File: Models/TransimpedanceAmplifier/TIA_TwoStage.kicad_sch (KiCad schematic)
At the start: 4 parts

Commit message: Save progress
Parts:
- added C_feedback: 80-220 fF, symbol Device:C
- R_feedback: renamed from R2; value 300M, 5% -> 330M, 5%; Purchase Link https://www.digikey.com/en/products/detail/vishay-dale/CRCW0603300MJPEAHR/5072019 -> https://www.digikey.com/en/products/detail/vishay-dale/CRCW0805330MJPEAHR/5074908
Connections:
- net at R_feedback.1: now also C_feedback.1
- net at R_feedback.2: now also C_feedback.2
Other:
- note added: "Noninverting Gain Stage Phase Shift: 0° Gain: 16.0 (-10 V < output < 10 V) 2.0 (outside ±10 V range)"
- moved on the sheet: RV1, RV2, RV3, R_feedback
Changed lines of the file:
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@@
 	(generator_version "9.0")
 	(paper "A4")
+	(text "Noninverting Gain Stage\n\nPhase Shift: 0°\n\nGain:\n16.0 (-10 V < output < 10 V)\n2.0 (outside ±10 V range)"
+		(exclude_from_sim no)
+		(at 152.908 67.818 0)
+		(effects
+			(font
+				(size 1.27 1.27)
+			)
+			(justify left)
+		)
+	)
+	(wire
+		(pts
+			(xy 77.47 53.34) (xy 73.66 53.34)
+		)
+		(stroke
+			(width 0)
+			(type default)
+		)
+	)
+	(wire
+		(pts
+			(xy 73.66 53.34) (xy 73.66 38.1)
+		)
+		(stroke
+			(width 0)
+			(type default)
+		)
+	)
+	(wire
+		(pts
+			(xy 73.66 38.1) (xy 77.47 38.1)
+		)
+		(stroke
+			(width 0)
+			(type default)
+		)
+	)
+	(wire
+		(pts
+			(xy 85.09 53.34) (xy 88.9 53.34)
+		)
+		(stroke
+			(width 0)
+			(type default)
+		)
+	)
+	(wire
+		(pts
+			(xy 85.09 38.1) (xy 88.9 38.1)
+		)
+		(stroke
+			(width 0)
+			(type default)
+		)
+	)
+	(wire
+		(pts
+			(xy 88.9 38.1) (xy 88.9 53.34)
+		)
+		(stroke
+			(width 0)
+			(type default)
+		)
+	)
+	(symbol
+		(lib_id "Device:C")
+		(at 81.28 38.1 90)
+		(unit 1)
+		(exclude_from_sim no)
+		(in_bom yes)
+		(on_board no)
+		(dnp no)
+		(fields_autoplaced yes)
+		(property "Reference" "C_feedback"
+			(at 81.28 30.48 90)
+			(effects
+				(font
+					(size 1.27 1.27)
+				)
+			)
+		)
+		(property "Value" "80-220 fF"
+			(at 81.28 33.02 90)
+			(effects
+				(font
+					(size 1.27 1.27)
+				)
+			)
+		)
+		(property "Footprint" ""
+			(at 85.09 37.1348 0)
+			(effects
+				(font
+					(size 1.27 1.27)
+				)
+				(hide yes)
+			)
+		)
+		(property "Datasheet" "~"
+			(at 81.28 38.1 0)
+			(effects
+				(font
+					(size 1.27 1.27)
+				)
+				(hide yes)
+			)
+		)
+		(property "Description" "Unpolarized capacitor"
+			(at 81.28 38.1 0)
+			(effects
+				(font
+					(size 1.27 1.27)
+				)
+				(hide yes)
+			)
+		)
+		(property "Purchase Link" ""
+			(at 81.28 38.1 0)
+			(effects
+				(font
+					(size 1.27 1.27)
+				)
+				(hide yes)
+			)
+		)
+		(pin "2"
+		)
+		(pin "1"
+		)
+		(instances
+			(project ""
+				(path "/ec9f2ae3-e40d-40eb-9760-2b611ee8efd1/226b3d0c-9e45-4bcf-9bef-58938aee743e"
+					(reference "C_feedback")
+					(unit 1)
+				)
+			)
+		)
+	)
 	(symbol
 		(lib_id "Device:R_US")
-		(at 91.44 53.34 0)
+		(at 81.28 53.34 90)
 		(unit 1)
 		(exclude_from_sim no)
@@
 		(dnp no)
 		(fields_autoplaced yes)
-		(property "Reference" "R2"
-			(at 93.98 52.0699 0)
-			(effects
-				(font
-					(size 1.27 1.27)
-				)
-				(justify left)
-			)
-		)
-		(property "Value" "300M, 5%"
-			(at 93.98 54.6099 0)
-			(effects
-				(font
-					(size 1.27 1.27)
-				)
-				(justify left)
+		(property "Reference" "R_feedback"
+			(at 81.28 46.99 90)
+			(effects
+				(font
+					(size 1.27 1.27)
+				)
+			)
+		)
+		(property "Value" "330M, 5%"
+			(at 81.28 49.53 90)
+			(effects
+				(font
+					(size 1.27 1.27)
+				)
 			)
 		)
 		(property "Footprint" ""
-			(at 92.456 53.594 90)
+			(at 81.534 52.324 90)
 			(effects
 				(font
@@
 		)
 		(property "Datasheet" "~"
-			(at 91.44 53.34 0)
+			(at 81.28 53.34 0)
 			(effects
 				(font
@@
 		)
 		(property "Description" "Resistor, US symbol"
-			(at 91.44 53.34 0)
-			(effects
-				(font
-					(size 1.27 1.27)
-				)
-				(hide yes)
-			)
-		)
-		(property "Purchase Link" "https://www.digikey.com/en/products/detail/vishay-dale/CRCW0603300MJPEAHR/5072019"
-			(at 91.44 53.34 0)
+			(at 81.28 53.34 0)
+			(effects
+				(font
+					(size 1.27 1.27)
+				)
+				(hide yes)
+			)
+		)
+		(property "Purchase Link" "https://www.digikey.com/en/products/detail/vishay-dale/CRCW0805330MJPEAHR/5074908"
+			(at 81.28 53.34 0)
 			(effects
 				(font
@@
 			(project ""
 				(path "/ec9f2ae3-e40d-40eb-9760-2b611ee8efd1/226b3d0c-9e45-4bcf-9bef-58938aee743e"
-					(reference "R2")
+					(reference "R_feedback")
 					(unit 1)
 				)
@@
 	(symbol
 		(lib_id "Device:R_Potentiometer_US")
-		(at 139.7 49.53 0)
+		(at 129.54 49.53 0)
 		(unit 1)
 		(exclude_from_sim no)
@@
 		(fields_autoplaced yes)
 		(property "Reference" "RV2"
-			(at 137.16 48.2599 0)
+			(at 127 48.2599 0)
 			(effects
 				(font
@@
 		)
 		(property "Value" "R_Potentiometer_US"
-			(at 137.16 50.7999 0)
+			(at 127 50.7999 0)
 			(effects
 				(font
@@
 		)
 		(property "Footprint" ""
-			(at 139.7 49.53 0)
+			(at 129.54 49.53 0)
 			(effects
 				(font
@@
 		)
 		(property "Datasheet" "~"
-			(at 139.7 49.53 0)
+			(at 129.54 49.53 0)
 			(effects
 				(font
@@
 		)
 		(property "Description" "Potentiometer, US symbol"
-			(at 139.7 49.53 0)
+			(at 129.54 49.53 0)
 			(effects
 				(font
@@
 	(symbol
 		(lib_id "Device:R_Potentiometer_US")
-		(at 139.7 62.23 0)
+		(at 129.54 62.23 0)
 		(unit 1)
 		(exclude_from_sim no)
@@
 		(fields_autoplaced yes)
 		(property "Reference" "RV3"
-			(at 137.16 60.9599 0)
+			(at 127 60.9599 0)
 			(effects
 				(font
@@
 		)
 		(property "Value" "R_Potentiometer_US"
-			(at 137.16 63.4999 0)
+			(at 127 63.4999 0)
 			(effects
 				(font
@@
 		)
 		(property "Footprint" ""
-			(at 139.7 62.23 0)
+			(at 129.54 62.23 0)
 			(effects
 				(font
@@
 		)
 		(property "Datasheet" "~"
-			(at 139.7 62.23 0)
+			(at 129.54 62.23 0)
 			(effects
 				(font
@@
 		)
 		(property "Description" "Potentiometer, US symbol"
-			(at 139.7 62.23 0)
+			(at 129.54 62.23 0)
 			(effects
 				(font
@@
 	(symbol
 		(lib_id "Device:R_Potentiometer_US")
-		(at 139.7 36.83 0)
+		(at 129.54 36.83 0)
 		(unit 1)
 		(exclude_from_sim no)
@@
 		(fields_autoplaced yes)
 		(property "Reference" "RV1"
-			(at 137.16 35.5599 0)
+			(at 127 35.5599 0)
 			(effects
 				(font
@@
 		)
 		(property "Value" "R_Potentiometer_US"
-			(at 137.16 38.0999 0)
+			(at 127 38.0999 0)
 			(effects
 				(font
@@
 		)
 		(property "Footprint" ""
-			(at 139.7 36.83 0)
+			(at 129.54 36.83 0)
 			(effects
 				(font
@@
 		)
 		(property "Datasheet" "~"
-			(at 139.7 36.83 0)
+			(at 129.54 36.83 0)
 			(effects
 				(font
@@
 		)
 		(property "Description" "Potentiometer, US symbol"
-			(at 139.7 36.83 0)
+			(at 129.54 36.83 0)
 			(effects
 				(font
@@
 	)
 	(sheet
-		(at 162.56 83.82)
+		(at 152.4 83.82)
 		(size 43.18 30.48)
 		(exclude_from_sim no)
@@
 		)
 		(property "Sheetname" "PostAmplifier"
-			(at 162.56 83.1084 0)
+			(at 152.4 83.1084 0)
 			(effects
 				(font
@@
 		)
 		(property "Sheetfile" "PostAmplifier.kicad_sch"
-			(at 162.56 114.8846 0)
+			(at 152.4 114.8846 0)
 			(effects
 				(font
@@
 	)
 	(sheet
-		(at 88.9 83.82)
+		(at 78.74 83.82)
 		(size 40.64 30.48)
 		(exclude_from_sim no)
@@
 		)
 		(property "Sheetname" "PreAmplifier"
-			(at 88.9 83.1084 0)
+			(at 78.74 83.1084 0)
 			(effects
 				(font
@@
 		)
 		(property "Sheetfile" "PreAmplifier.kicad_sch"
-			(at 88.9 114.8846 0)
-			(effects
-				(font
+			(at 78.74 114.8846 0)
+			(effects
+				(font

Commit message: Save progress
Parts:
- removed RV1, RV2, RV3: R_Potentiometer_US, symbol Device:R_Potentiometer_US
- added C_main_comp, C_midf_comp: TBD, symbol Device:C
- added R_bandwidth, R_main_comp, R_midf_comp: TBD, symbol Device:R_Variable_US
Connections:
- net Input: now reaches C_feedback.1, R_feedback.1
- net at C_feedback.2, R_feedback.2: now also C_main_comp.1, R_main_comp.1, R_midf_comp.1
- new net: C_main_comp.2, R_bandwidth.1
- new net: C_midf_comp.1, R_midf_comp.2
- new net GND: R_bandwidth.2
- new net Output: C_midf_comp.2, R_main_comp.2
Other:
- sheet PostAmplifier ports: added -15V, 15V, Input, Output; removed none
- sheet PreAmplifier ports: added -5V, 5V, Input, Output; removed none
- moved on the sheet: C_feedback, R_feedback

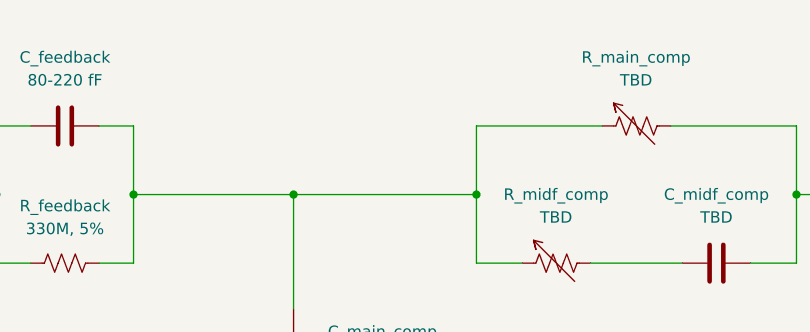
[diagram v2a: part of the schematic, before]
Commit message: Fully specified the high-level connections between subsystems
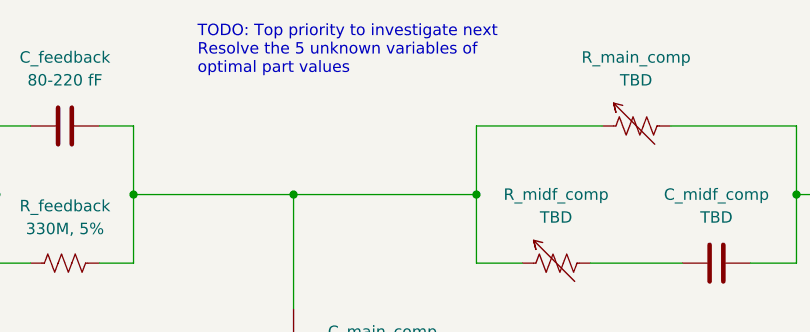
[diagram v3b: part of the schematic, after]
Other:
- note added: "TODO: Top priority to investigate next Resolve the 5 unknown variables of optimal part values"
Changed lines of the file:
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@@
 	(generator_version "9.0")
 	(paper "A4")
+	(text "TODO: Top priority to investigate next\nResolve the 5 unknown variables of\noptimal part values"
+		(exclude_from_sim no)
+		(at 83.312 21.844 0)
+		(effects
+			(font
+				(size 1.27 1.27)
+			)
+			(justify left top)
+		)
+	)
 	(text "Noninverting Gain Stage\n\nPhase Shift: 0°\n\nGain:\n16.0 (-10 V < output < 10 V)\n2.0 (outside ±10 V range)"
 		(exclude_from_sim no)

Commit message: Save progress
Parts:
- added R_bandwidth_fixed: R_US, symbol Device:R_US
- renumbered R_bandwidth to R_bandwidth_trim
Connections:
- net GND: no longer R_bandwidth_trim.2
- net Output: no longer C_midf_comp.2, R_main_comp.2
- net at C_main_comp.2: no longer R_bandwidth_trim.1
- new net: C_midf_comp.2, R_main_comp.2
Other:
- note added: "Conservative constraint for loop stability 5.1 kHz << f_bandwidth < 61 kHz 1304 Ω < R_bandwidth << 15.6 kΩ Achievable resistance range Lower bound of uncertainty: 1337 Ω - 10.3 kΩ Upper bound of uncertainty: 1423 Ω - 12.3 kΩ"
- note added: "Tunability of R_bandwidth to one simulated optimal resistance 0.05% (A_R of trimpot) 0.07% (upper bound of uncertainty for optimal R) 0.22% (lower bound of uncertainty for optimal R)"
- note removed: "TODO: Top priority to investigate next Resolve the 5 unknown variables of optimal part values"
- moved on the sheet: R_bandwidth_trim
